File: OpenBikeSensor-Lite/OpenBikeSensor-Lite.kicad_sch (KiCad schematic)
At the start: 4 parts, among them J1 Sensor A, J2 Sensor B, J3 I2C Extension, U1 ESP32-DEVKIT-32C

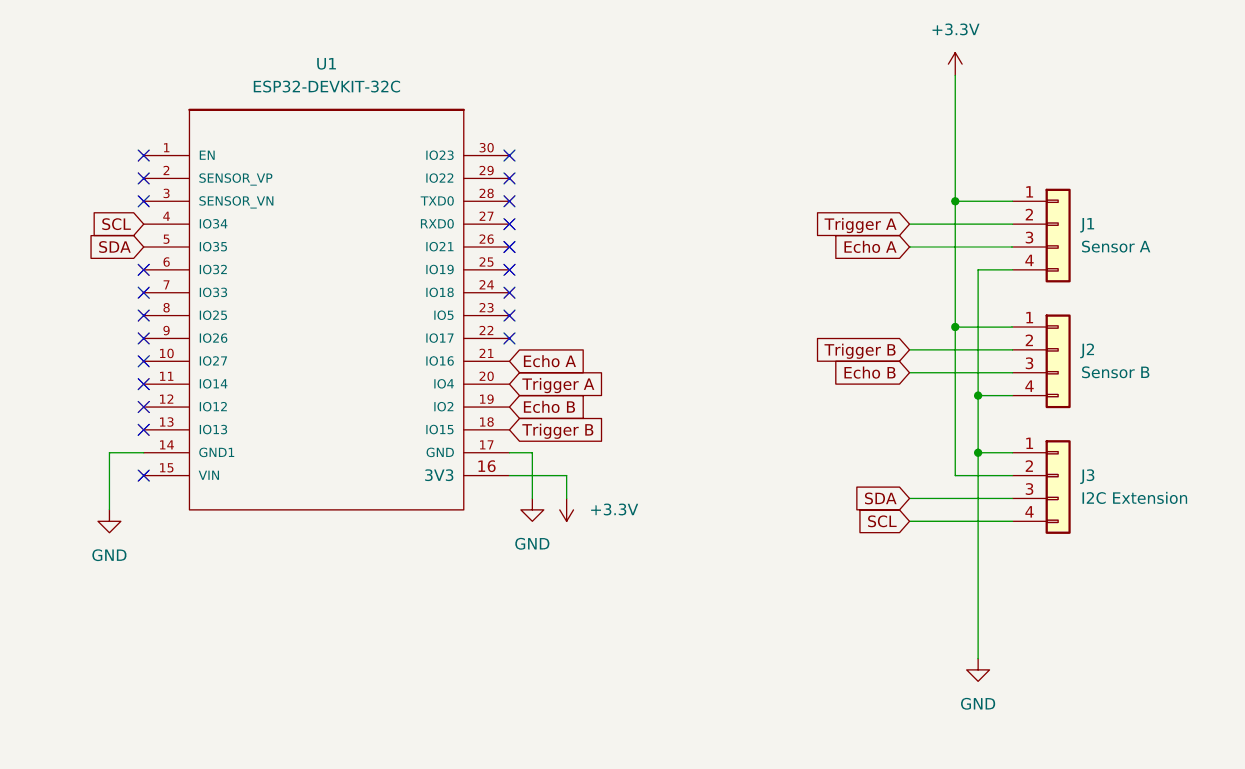
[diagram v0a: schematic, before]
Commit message: lite: Add button, add GND on voltage pin, change pinout to same as normal OBS
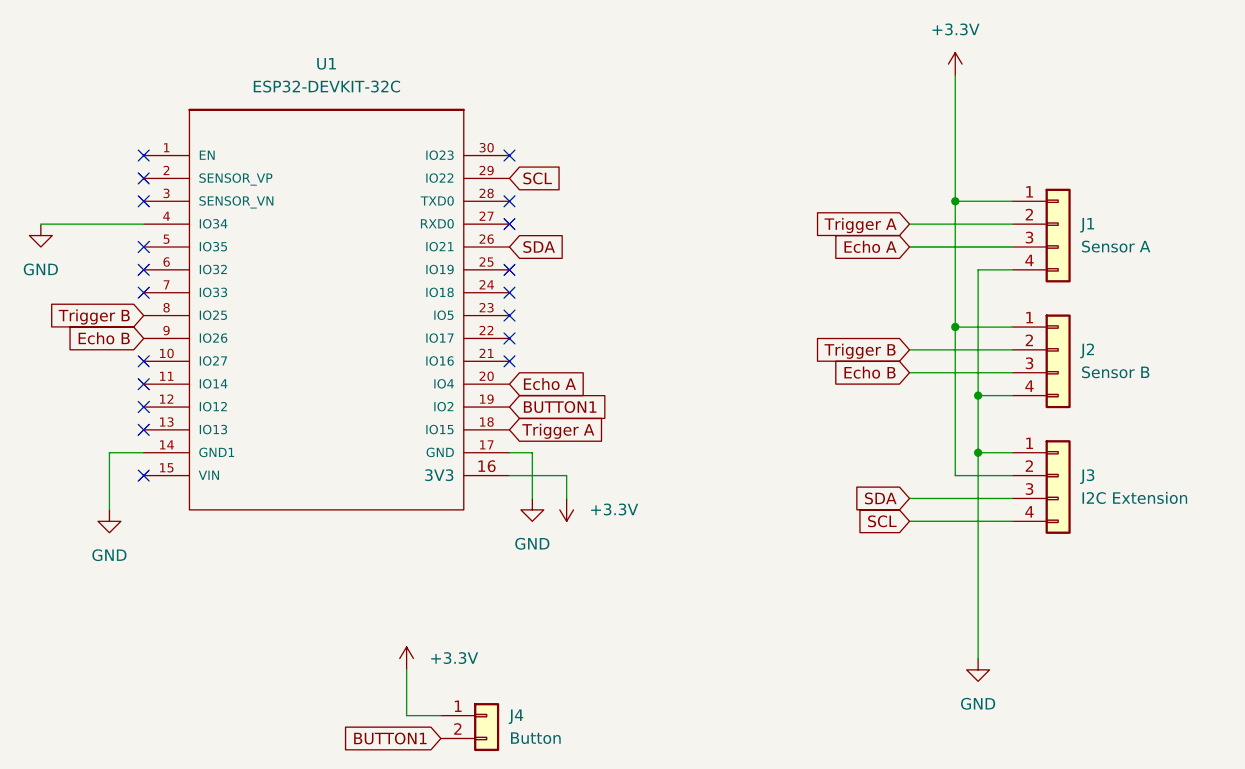
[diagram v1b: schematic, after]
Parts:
- added J4: Button, Connector_JST:JST_EH_S2B-EH_1x02_P2.50mm_Horizontal, symbol Connector_Generic:Conn_01x02
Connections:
- net +3V3: now also J4.1 (Pin_1)
- net Echo A: now also U1.20 (IO4); no longer U1.21 (IO16)
- net Echo B: now also U1.9 (IO26); no longer U1.19 (IO2)
- net GND: now also U1.4 (IO34)
- net SCL: now also U1.29 (IO22); no longer U1.4 (IO34)
- net SDA: now also U1.26 (IO21); no longer U1.5 (IO35)
- net Trigger A: now also U1.18 (IO15); no longer U1.20 (IO4)
- net Trigger B: now also U1.8 (IO25); no longer U1.18 (IO15)
- new net BUTTON1: J4.2 (Pin_2), U1.19 (IO2)
- no-connect marks 21 -> 19
